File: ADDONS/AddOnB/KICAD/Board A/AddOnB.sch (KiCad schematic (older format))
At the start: 136 parts, among them IC1 FIN1002, IC101 74HC251, IC2 FIN1002, IC3 FIN1002, IC4 FIN1002, IC5 IC_NCP1117LPST33, IC6 PCA9536D, SW101 SW_DIP_x08, X1 RCA, X101 XLR3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

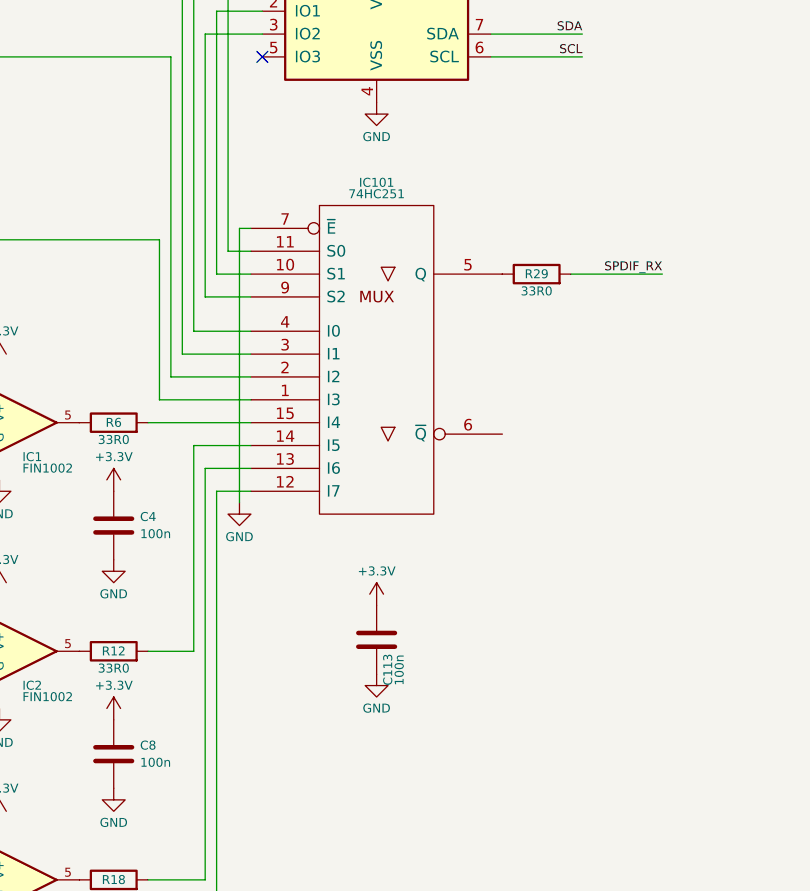
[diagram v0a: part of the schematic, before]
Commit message: Bugfix: +3V3 connection on multiplexer
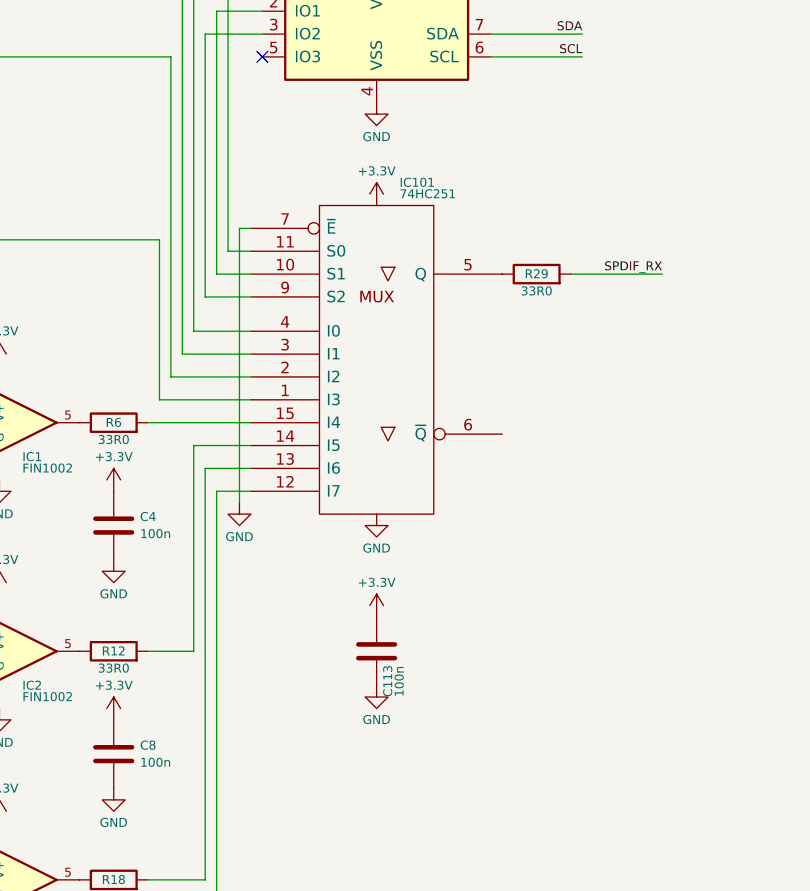
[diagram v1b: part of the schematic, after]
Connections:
- net VCC is gone; now on net +3V3: IC101.16 (VCC)
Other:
- moved on the sheet: C113
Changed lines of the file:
@@
 EESchema Schematic File Version 4
 LIBS:AddOnB-cache
-EELAYER 26 0
+EELAYER 29 0
 EELAYER END
 $Descr A3 16535 11693
@@
 U 1 1 5C904A11
 P 8250 4550
-F 0 "IC101" H 8250 5300 39  0000 C CNN
-F 1 "74HC251" H 8250 5250 39  0000 C CNN
+F 0 "IC101" H 8350 5300 39  0000 L CNN
+F 1 "74HC251" H 8350 5250 39  0000 L CNN
 F 2 "Package_SO:SOIC-16_3.9x9.9mm_P1.27mm" H 8250 4550 50  0001 C CNN
 F 3 "" H 8250 4550 50  0001 C CNN
@@
 L power:GND #PWR0126
 U 1 1 5C9BD6F3
-P 8250 5950
-F 0 "#PWR0126" H 8250 5700 50  0001 C CNN
-F 1 "GND" H 8250 5800 39  0000 C CNN
-F 2 "" H 8250 5950 50  0001 C CNN
-F 3 "" H 8250 5950 50  0001 C CNN
-	1    8250 5950
+P 8250 6000
+F 0 "#PWR0126" H 8250 5750 50  0001 C CNN
+F 1 "GND" H 8250 5850 39  0000 C CNN
+F 2 "" H 8250 6000 50  0001 C CNN
+F 3 "" H 8250 6000 50  0001 C CNN
+	1    8250 6000
 	1    0    0    -1
 $EndComp
@@
 L rk:CAP_100n_50V_X7R_0805 C113
 U 1 1 5C9C6233
-P 8250 5800
-F 0 "C113" H 8050 5750 39  0000 L CNN
-F 1 "CAP_100n_50V_X7R_0805" H 8250 5650 39  0001 C CNN
-F 2 "rklib:C0805-X7R" H 8250 5600 39  0001 C CNN
-F 3 "" H 8300 5850 50  0001 C CNN
-F 4 "100n" H 8050 5700 39  0000 L CNN "Value1"
-F 5 "5% 50V X7R" H 8250 5550 39  0001 C CNN "Value2"
-F 6 "399-1170-1-ND" H 8250 5500 39  0001 C CNN "digikey"
-	1    8250 5800
+P 8250 5850
+F 0 "C113" H 8050 5800 39  0000 L CNN
+F 1 "CAP_100n_50V_X7R_0805" H 8250 5700 39  0001 C CNN
+F 2 "rklib:C0805-X7R" H 8250 5650 39  0001 C CNN
+F 3 "" H 8300 5900 50  0001 C CNN
+F 4 "100n" H 8050 5750 39  0000 L CNN "Value1"
+F 5 "5% 50V X7R" H 8250 5600 39  0001 C CNN "Value2"
+F 6 "399-1170-1-ND" H 8250 5550 39  0001 C CNN "digikey"
+	1    8250 5850
 	0    -1   -1   0
 $EndComp
@@
 L power:+3.3V #PWR0124
 U 1 1 5C9CE791
-P 8250 5650
-F 0 "#PWR0124" H 8250 5500 50  0001 C CNN
-F 1 "+3.3V" H 8250 5800 39  0000 C CNN
-F 2 "" H 8250 5650 50  0001 C CNN
-F 3 "" H 8250 5650 50  0001 C CNN
-	1    8250 5650
+P 8250 5700
+F 0 "#PWR0124" H 8250 5550 50  0001 C CNN
+F 1 "+3.3V" H 8250 5850 39  0000 C CNN
+F 2 "" H 8250 5700 50  0001 C CNN
+F 3 "" H 8250 5700 50  0001 C CNN
+	1    8250 5700
 	1    0    0    -1
 $EndComp
@@
 Wire Wire Line
 	2000 6200 1700 6200
+$Comp
+L power:GND #PWR?
+U 1 1 5CBED130
+P 8250 5250
+F 0 "#PWR?" H 8250 5000 50  0001 C CNN
+F 1 "GND" H 8250 5100 39  0000 C CNN
+F 2 "" H 8250 5250 50  0001 C CNN
+F 3 "" H 8250 5250 50  0001 C CNN
+	1    8250 5250
+	1    0    0    -1
+$EndComp
+$Comp
+L power:+3.3V #PWR?
+U 1 1 5CC232CF
+P 8250 3900
+F 0 "#PWR?" H 8250 3750 50  0001 C CNN
+F 1 "+3.3V" H 8250 4050 39  0000 C CNN
+F 2 "" H 8250 3900 50  0001 C CNN
+F 3 "" H 8250 3900 50  0001 C CNN
+	1    8250 3900
+	1    0    0    -1
+$EndComp
 $EndSCHEMATC

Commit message: Updated documentation
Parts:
- C1, C10, C109, C11, C110, C111, C112, C113, C12, C13, C14, C15, C16, C2, C24, C3, C4, C5, C6, C7, C8, C9: Manufacturer (none) -> KEMET; pn (none) -> C0805C104K5RACTU
- C101, C102, C103, C104, C105, C106, C107, C108: Manufacturer (none) -> KEMET; pn (none) -> C0805C101J5GACTU
- C17, C18, C19, C20: Manufacturer (none) -> Yageo; pn (none) -> CC0805KRX7R9BB103
- D1, D2, D3, D4: Manufacturer (none) -> Littelfuse Inc.; pn (none) -> PESD0603-240
- IC1, IC2, IC3, IC4: Manufacturer (none) -> ON Semiconductor; pn (none) -> FIN1002M5X
- IC101: Manufacturer (none) -> Texas Instruments; pn (none) -> SN74HC251DR
- IC6: Manufacturer (none) -> Texas Instruments; pn (none) -> PCA9536DR
- L101, L102, L103, L104: Manufacturer (none) -> Taiyo Yuden; pn (none) -> LBR2012T470K
- R1, R13, R19, R7: Manufacturer (none) -> Yageo; pn (none) -> RC0805FR-0791RL
- R10, R11, R15, R16, R17, R21, R22, R23, R3, R4, R5, R9: Manufacturer (none) -> Yageo; pn (none) -> RC0805FR-07470RL
- R101, R102, R103, R104, R105, R106, R107, R108, R109, R110, R111, R112, R113, R114, R115, R116: value RES_68R0_1%_0.125W_Thick_0805 -> RES_68R0_1%_0.125W_Thin_0805; Manufacturer (none) -> Panasonic Electronic Components; pn (none) -> ERA-6AED680V
- R117, R119, R121, R123, R125, R127, R129, R131: Manufacturer (none) -> Stackpole Electronics Inc; pn (none) -> RNCP0805FTD100R
- R118, R120, R122, R124, R126, R128, R130, R132: Manufacturer (none) -> Yageo; pn (none) -> RC0805FR-07220KL
- R12, R18, R24, R29, R6: Manufacturer (none) -> Yageo; pn (none) -> RC0805FR-0733RL
- R14, R2, R20, R8: Manufacturer (none) -> Yageo; pn (none) -> RC0805FR-07820RL
- R25, R26, R27, R28: Manufacturer (none) -> Yageo; pn (none) -> RC0805FR-0710KL
- SW101: Manufacturer (none) -> E-Switch; pn (none) -> KAS2108ET
- X1, X2, X3, X4: Manufacturer (none) -> Switchcraft Inc.; pn (none) -> PJRAN1X1U01AUX
- X101, X102, X103, X104, X105, X106, X107, X108: Manufacturer (none) -> Neutrik; pn (none) -> NC3MAH-0
- X109: Manufacturer (none) -> Switchcraft Inc.; pn (none) -> PJRAS4X2U01AUX
- X110, X111, X112, X113: Manufacturer (none) -> Everlight Electronics Co Ltd; pn (none) -> PLR135/T10
- X114, X115: Manufacturer (none) -> Bud Industries; pn (none) -> BC-32677
- X5: Manufacturer (none) -> TE Connectivity AMP Connectors; Value1 (none) -> MicroMatch-14; Value2 (none) -> -; pn (none) -> 1-215079-4
- X6: Manufacturer (none) -> On Shore Technology Inc.; pn (none) -> 302-S161

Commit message: Reversed X5
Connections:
- net GND: now also X5.2 (Pin_2); no longer X5.14 (Pin_14)
- net OPTICAL_RX: now also X5.9 (Pin_9); no longer X5.5 (Pin_5)
- net OPTICAL_TX: now also X5.11 (Pin_11); no longer X5.3 (Pin_3)
- net SPDIF_RX: now also X5.1 (Pin_1); no longer X5.13 (Pin_13)
- net SPDIF_TX: now also X5.3 (Pin_3); no longer X5.11 (Pin_11)
- net WCLK_RX: now also X5.5 (Pin_5); no longer X5.9 (Pin_9)
- net +12V renamed VPP
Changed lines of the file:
@@
-	1    0    0    -1
-$EndComp
-$Comp
-L power:+12V #PWR042
-U 1 1 5CA1EA3A
-P 10700 8150
-F 0 "#PWR042" H 10700 8000 50  0001 C CNN
-F 1 "+12V" H 10700 8300 39  0000 C CNN
-F 2 "" H 10700 8150 50  0001 C CNN
-F 3 "" H 10700 8150 50  0001 C CNN
-	1    10700 8150
 	1    0    0    -1
 $EndComp
@@
 	11450 6250 11450 6350
 $Comp
-L power:+12V #PWR040
-U 1 1 5C99954F
-P 10850 6100
-F 0 "#PWR040" H 10850 5950 50  0001 C CNN
-F 1 "+12V" H 10850 6250 39  0000 C CNN
-F 2 "" H 10850 6100 50  0001 C CNN
-F 3 "" H 10850 6100 50  0001 C CNN
-	1    10850 6100
-	1    0    0    -1
-$EndComp
-$Comp
 L power:GND #PWR039
 U 1 1 5C9C64B2
@@
 F 7 "1-215079-4" H 0   0   50  0001 C CNN "pn"
 	1    11100 5300
-	1    0    0    -1
+	1    0    0    1
 $EndComp
 $Comp
@@
 	2650 5600 2650 5700
 $Comp
-L power:GND #PWR?
+L power:GND #PWR0136
 U 1 1 5C942FF1
 P 2650 6250
-F 0 "#PWR?" H 2650 6000 50  0001 C CNN
+F 0 "#PWR0136" H 2650 6000 50  0001 C CNN
 F 1 "GND" H 2650 6100 39  0000 C CNN
 F 2 "" H 2650 6250 50  0001 C CNN
@@
 	2000 6200 1700 6200
 $Comp
-L power:GND #PWR?
+L power:GND #PWR0143
 U 1 1 5CBED130
 P 8250 5250
-F 0 "#PWR?" H 8250 5000 50  0001 C CNN
+F 0 "#PWR0143" H 8250 5000 50  0001 C CNN
 F 1 "GND" H 8250 5100 39  0000 C CNN
 F 2 "" H 8250 5250 50  0001 C CNN
@@
 $EndComp
 $Comp
-L power:+3.3V #PWR?
+L power:+3.3V #PWR0144
 U 1 1 5CC232CF
 P 8250 3900
-F 0 "#PWR?" H 8250 3750 50  0001 C CNN
+F 0 "#PWR0144" H 8250 3750 50  0001 C CNN
 F 1 "+3.3V" H 8250 4050 39  0000 C CNN
 F 2 "" H 8250 3900 50  0001 C CNN
@@
 	1    0    0    -1
 $EndComp
+$Comp
+L power:VPP #PWR0145
+U 1 1 5DB8FD8A
+P 10700 8150
+F 0 "#PWR0145" H 10700 8000 50  0001 C CNN
+F 1 "VPP" H 10700 8300 39  0000 C CNN
+F 2 "" H 10700 8150 50  0001 C CNN
+F 3 "" H 10700 8150 50  0001 C CNN
+	1    10700 8150
+	1    0    0    -1
+$EndComp
+$Comp
+L power:VPP #PWR0147
+U 1 1 5DBC9401
+P 10850 6100
+F 0 "#PWR0147" H 10850 5950 50  0001 C CNN
+F 1 "VPP" H 10850 6250 39  0000 C CNN
+F 2 "" H 10850 6100 50  0001 C CNN
+F 3 "" H 10850 6100 50  0001 C CNN
+	1    10850 6100
+	1    0    0    -1
+$EndComp

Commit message: Updated BOMs
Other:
- note removed: "TODO VCC vs +3V3"
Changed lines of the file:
@@
 Wire Wire Line
 	7450 1650 7450 4450
-Text Notes 10650 9350 0    197  ~ 0
-TODO VCC vs +3V3
 $Comp
 L rk:RES_33R0_1%_0.125W_Thick_0805 R29

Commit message: Added 4FIRs plugin to GUI
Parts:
- R117, R119, R121, R123, R125, R127, R129, R131: value RES_100R_1%_0.25W_Thin_0805 -> RES_100R_0.5%_0.100W_Thin_0805; Manufacturer Stackpole Electronics Inc -> Susumu; Value2 1% 0.25W Thin -> 0.5% 0.100W Thin; pn RNCP0805FTD100R -> RR1220P-101-D
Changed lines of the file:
@@
 P 2350 1200
 F 0 "R117" H 2350 1200 39  0000 C CNN
-F 1 "RES_100R_1%_0.25W_Thin_0805" H 2350 1025 39  0001 C CNN
+F 1 "RES_100R_0.5%_0.100W_Thin_0805" H 2350 1025 39  0001 C CNN
 F 2 "rklib:C0805-RES" H 2350 975 39  0001 C CNN
 F 3 "" H 2350 1200 50  0000 C CNN
 F 4 "100R" H 2350 1125 39  0000 C CNN "Value1"
-F 5 "1% 0.25W Thin" H 2350 1075 39  0001 C CNN "Value2"
+F 5 "0.5% 0.100W Thin" H 2350 1075 39  0001 C CNN "Value2"
 F 6 "RNCP0805FTD100RCT-ND" H 2350 900 39  0001 C CNN "digikey"
-F 7 "Stackpole Electronics Inc" H 0   0   50  0001 C CNN "Manufacturer"
-F 8 "RNCP0805FTD100R" H 0   0   50  0001 C CNN "pn"
+F 7 "Susumu" H 0   0   50  0001 C CNN "Manufacturer"
+F 8 "RR1220P-101-D" H 0   0   50  0001 C CNN "pn"
 	1    2350 1200
 	1    0    0    -1
@@
 P 2350 1600
 F 0 "R119" H 2350 1600 39  0000 C CNN
-F 1 "RES_100R_1%_0.25W_Thin_0805" H 2350 1425 39  0001 C CNN
+F 1 "RES_100R_0.5%_0.100W_Thin_0805" H 2350 1425 39  0001 C CNN
 F 2 "rklib:C0805-RES" H 2350 1375 39  0001 C CNN
 F 3 "" H 2350 1600 50  0000 C CNN
 F 4 "100R" H 2350 1525 39  0000 C CNN "Value1"
-F 5 "1% 0.25W Thin" H 2350 1475 39  0001 C CNN "Value2"
+F 5 "0.5% 0.100W Thin" H 2350 1475 39  0001 C CNN "Value2"
 F 6 "RNCP0805FTD100RCT-ND" H 2350 1300 39  0001 C CNN "digikey"
-F 7 "Stackpole Electronics Inc" H 0   0   50  0001 C CNN "Manufacturer"
-F 8 "RNCP0805FTD100R" H 0   0   50  0001 C CNN "pn"
+F 7 "Susumu" H 0   0   50  0001 C CNN "Manufacturer"
+F 8 "RR1220P-101-D" H 0   0   50  0001 C CNN "pn"
 	1    2350 1600
 	1    0    0    -1
@@
 P 2350 2150
 F 0 "R121" H 2350 2150 39  0000 C CNN
-F 1 "RES_100R_1%_0.25W_Thin_0805" H 2350 1975 39  0001 C CNN
+F 1 "RES_100R_0.5%_0.100W_Thin_0805" H 2350 1975 39  0001 C CNN
 F 2 "rklib:C0805-RES" H 2350 1925 39  0001 C CNN
 F 3 "" H 2350 2150 50  0000 C CNN
 F 4 "100R" H 2350 2075 39  0000 C CNN "Value1"
-F 5 "1% 0.25W Thin" H 2350 2025 39  0001 C CNN "Value2"
+F 5 "0.5% 0.100W Thin" H 2350 2025 39  0001 C CNN "Value2"
 F 6 "RNCP0805FTD100RCT-ND" H 2350 1850 39  0001 C CNN "digikey"
-F 7 "Stackpole Electronics Inc" H 0   0   50  0001 C CNN "Manufacturer"
-F 8 "RNCP0805FTD100R" H 0   0   50  0001 C CNN "pn"
+F 7 "Susumu" H 0   0   50  0001 C CNN "Manufacturer"
+F 8 "RR1220P-101-D" H 0   0   50  0001 C CNN "pn"
 	1    2350 2150
 	1    0    0    -1
@@
 P 2350 2550
 F 0 "R123" H 2350 2550 39  0000 C CNN
-F 1 "RES_100R_1%_0.25W_Thin_0805" H 2350 2375 39  0001 C CNN
+F 1 "RES_100R_0.5%_0.100W_Thin_0805" H 2350 2375 39  0001 C CNN
 F 2 "rklib:C0805-RES" H 2350 2325 39  0001 C CNN
 F 3 "" H 2350 2550 50  0000 C CNN
 F 4 "100R" H 2350 2475 39  0000 C CNN "Value1"
-F 5 "1% 0.25W Thin" H 2350 2425 39  0001 C CNN "Value2"
+F 5 "0.5% 0.100W Thin" H 2350 2425 39  0001 C CNN "Value2"
 F 6 "RNCP0805FTD100RCT-ND" H 2350 2250 39  0001 C CNN "digikey"
-F 7 "Stackpole Electronics Inc" H 0   0   50  0001 C CNN "Manufacturer"
-F 8 "RNCP0805FTD100R" H 0   0   50  0001 C CNN "pn"
+F 7 "Susumu" H 0   0   50  0001 C CNN "Manufacturer"
+F 8 "RR1220P-101-D" H 0   0   50  0001 C CNN "pn"
 	1    2350 2550
 	1    0    0    -1
@@
 P 2350 3100
 F 0 "R125" H 2350 3100 39  0000 C CNN
-F 1 "RES_100R_1%_0.25W_Thin_0805" H 2350 2925 39  0001 C CNN
+F 1 "RES_100R_0.5%_0.100W_Thin_0805" H 2350 2925 39  0001 C CNN
 F 2 "rklib:C0805-RES" H 2350 2875 39  0001 C CNN
 F 3 "" H 2350 3100 50  0000 C CNN
 F 4 "100R" H 2350 3025 39  0000 C CNN "Value1"
-F 5 "1% 0.25W Thin" H 2350 2975 39  0001 C CNN "Value2"
+F 5 "0.5% 0.100W Thin" H 2350 2975 39  0001 C CNN "Value2"
 F 6 "RNCP0805FTD100RCT-ND" H 2350 2800 39  0001 C CNN "digikey"
-F 7 "Stackpole Electronics Inc" H 0   0   50  0001 C CNN "Manufacturer"
-F 8 "RNCP0805FTD100R" H 0   0   50  0001 C CNN "pn"
+F 7 "Susumu" H 0   0   50  0001 C CNN "Manufacturer"
+F 8 "RR1220P-101-D" H 0   0   50  0001 C CNN "pn"
 	1    2350 3100
 	1    0    0    -1
@@
 P 2350 3500
 F 0 "R127" H 2350 3500 39  0000 C CNN
-F 1 "RES_100R_1%_0.25W_Thin_0805" H 2350 3325 39  0001 C CNN
+F 1 "RES_100R_0.5%_0.100W_Thin_0805" H 2350 3325 39  0001 C CNN
 F 2 "rklib:C0805-RES" H 2350 3275 39  0001 C CNN
 F 3 "" H 2350 3500 50  0000 C CNN
 F 4 "100R" H 2350 3425 39  0000 C CNN "Value1"
-F 5 "1% 0.25W Thin" H 2350 3375 39  0001 C CNN "Value2"
+F 5 "0.5% 0.100W Thin" H 2350 3375 39  0001 C CNN "Value2"
 F 6 "RNCP0805FTD100RCT-ND" H 2350 3200 39  0001 C CNN "digikey"
-F 7 "Stackpole Electronics Inc" H 0   0   50  0001 C CNN "Manufacturer"
-F 8 "RNCP0805FTD100R" H 0   0   50  0001 C CNN "pn"
+F 7 "Susumu" H 0   0   50  0001 C CNN "Manufacturer"
+F 8 "RR1220P-101-D" H 0   0   50  0001 C CNN "pn"
 	1    2350 3500
 	1    0    0    -1
@@
 P 2350 4050
 F 0 "R129" H 2350 4050 39  0000 C CNN
-F 1 "RES_100R_1%_0.25W_Thin_0805" H 2350 3875 39  0001 C CNN
+F 1 "RES_100R_0.5%_0.100W_Thin_0805" H 2350 3875 39  0001 C CNN
 F 2 "rklib:C0805-RES" H 2350 3825 39  0001 C CNN
 F 3 "" H 2350 4050 50  0000 C CNN
 F 4 "100R" H 2350 3975 39  0000 C CNN "Value1"
-F 5 "1% 0.25W Thin" H 2350 3925 39  0001 C CNN "Value2"
+F 5 "0.5% 0.100W Thin" H 2350 3925 39  0001 C CNN "Value2"
 F 6 "RNCP0805FTD100RCT-ND" H 2350 3750 39  0001 C CNN "digikey"
-F 7 "Stackpole Electronics Inc" H 0   0   50  0001 C CNN "Manufacturer"
-F 8 "RNCP0805FTD100R" H 0   0   50  0001 C CNN "pn"
+F 7 "Susumu" H 0   0   50  0001 C CNN "Manufacturer"
+F 8 "RR1220P-101-D" H 0   0   50  0001 C CNN "pn"
 	1    2350 4050
 	1    0    0    -1
@@
 P 2350 4450
 F 0 "R131" H 2350 4450 39  0000 C CNN
-F 1 "RES_100R_1%_0.25W_Thin_0805" H 2350 4275 39  0001 C CNN
+F 1 "RES_100R_0.5%_0.100W_Thin_0805" H 2350 4275 39  0001 C CNN
 F 2 "rklib:C0805-RES" H 2350 4225 39  0001 C CNN
 F 3 "" H 2350 4450 50  0000 C CNN
 F 4 "100R" H 2350 4375 39  0000 C CNN "Value1"
-F 5 "1% 0.25W Thin" H 2350 4325 39  0001 C CNN "Value2"
+F 5 "0.5% 0.100W Thin" H 2350 4325 39  0001 C CNN "Value2"
 F 6 "RNCP0805FTD100RCT-ND" H 2350 4150 39  0001 C CNN "digikey"
-F 7 "Stackpole Electronics Inc" H 0   0   50  0001 C CNN "Manufacturer"
-F 8 "RNCP0805FTD100R" H 0   0   50  0001 C CNN "pn"
+F 7 "Susumu" H 0   0   50  0001 C CNN "Manufacturer"
+F 8 "RR1220P-101-D" H 0   0   50  0001 C CNN "pn"
 	1    2350 4450
 	1    0    0    -1

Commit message: PDF schematic AddOn B
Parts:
- IC6: symbol Interface_Expansion:PCA9536D -> AddOnB-rescue:PCA9536D-Interface_Expansion
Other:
- note added: "Connect to X101 on Aurora mainboard."
- note added: "Connect to X102 on Aurora mainboard."
- note added: "Connect to X201 on Aurora mainboard\nand to X109 on \nXLR Input Board (Board B).\nDaisy chain X109 -> X114 -> X201\nor X114 -> X109 -> X201"
- note added: "Connect to X301 on Aurora mainboard."
- note added: "Termination of cold Input.\nTurn on for the channels connected by RCA.\nDon’t connect an external signal to the XLRs \nfor these channels."
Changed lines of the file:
@@
 EESchema Schematic File Version 4
-LIBS:AddOnB-cache
-EELAYER 29 0
+EELAYER 30 0
 EELAYER END
 $Descr A3 16535 11693
 encoding utf-8
 Sheet 1 1
-Title ""
+Title "AddOn B Board A"
 Date ""
 Rev ""
-Comp ""
+Comp "auverdion"
 Comment1 ""
 Comment2 ""
@@
 SPDIF_RX
 $Comp
-L Interface_Expansion:PCA9536D IC6
+L AddOnB-rescue:PCA9536D-Interface_Expansion IC6
 U 1 1 5CA2E908
 P 8250 3050
@@
 	1    0    0    -1
 $EndComp
+Text Notes 11750 2450 0    79   ~ 0
+Connect to X201 on Aurora mainboard\nand to X109 on \nXLR Input Board (Board B).\nDaisy chain X109 -> X114 -> X201\nor X114 -> X109 -> X201
+Text Notes 11750 3900 0    79   ~ 0
+Connect to X301 on Aurora mainboard.
+Text Notes 11550 5350 0    79   ~ 0
+Connect to X101 on Aurora mainboard.
+Text Notes 11550 6550 0    79   ~ 0
+Connect to X102 on Aurora mainboard.
+Text Notes 1200 7000 0    79   ~ 0
+Termination of cold Input.\nTurn on for the channels connected by RCA.\nDon’t connect an external signal to the XLRs \nfor these channels.
 $EndSCHEMATC
